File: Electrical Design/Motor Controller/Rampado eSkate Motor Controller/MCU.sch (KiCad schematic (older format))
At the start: 12 parts

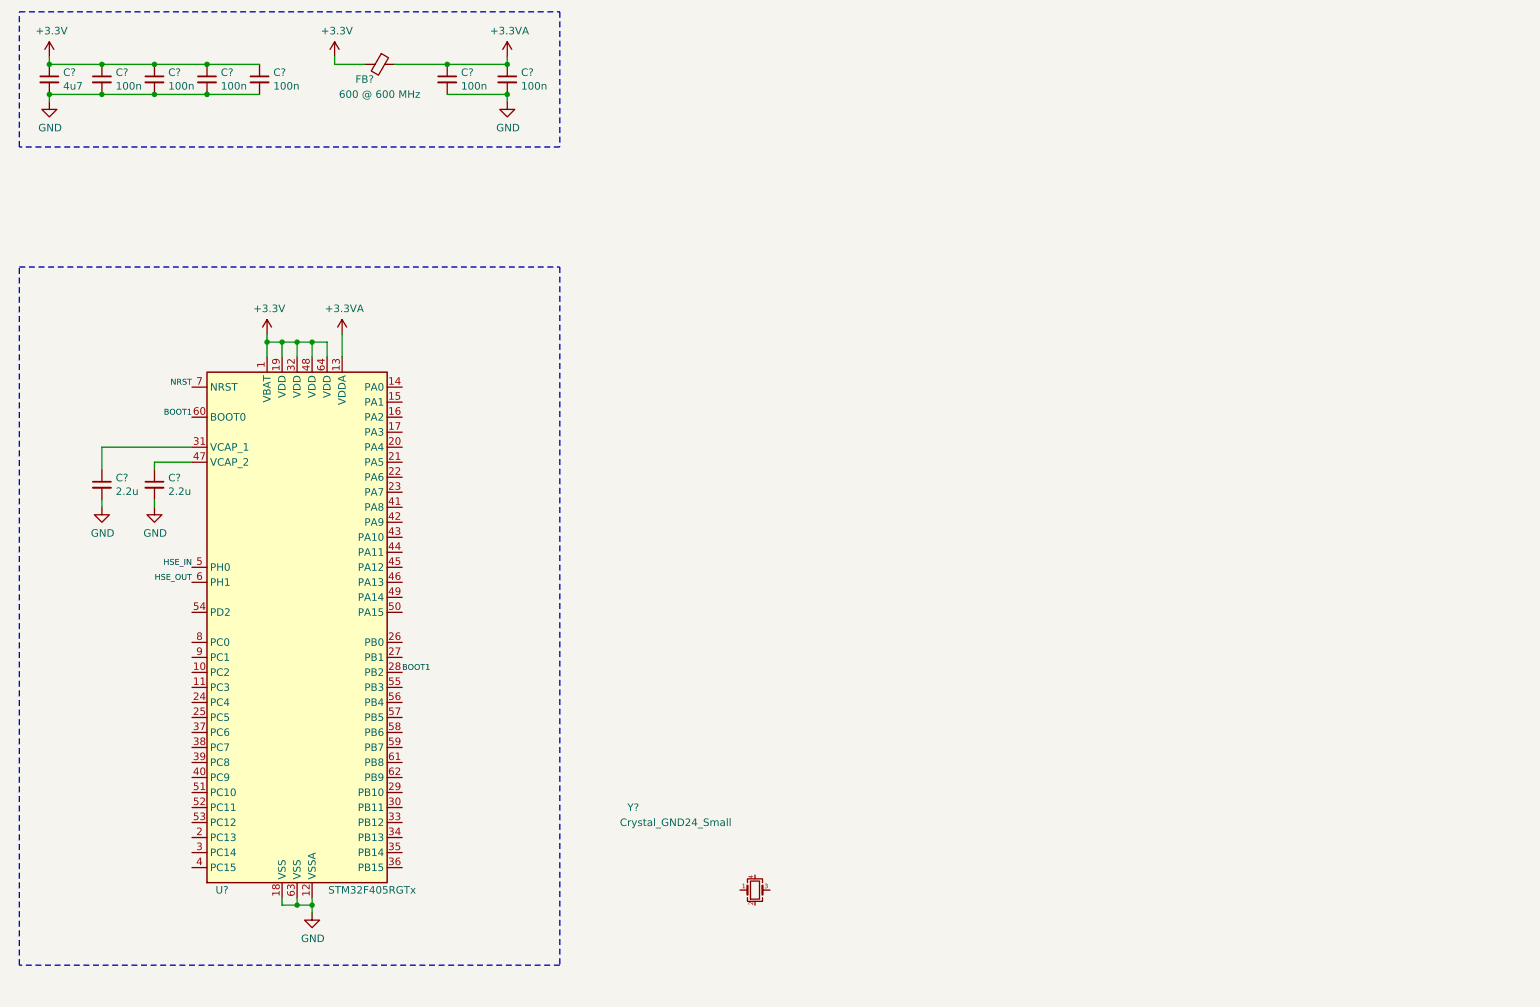
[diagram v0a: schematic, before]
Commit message: Finished USB and started peripherals for motor controller
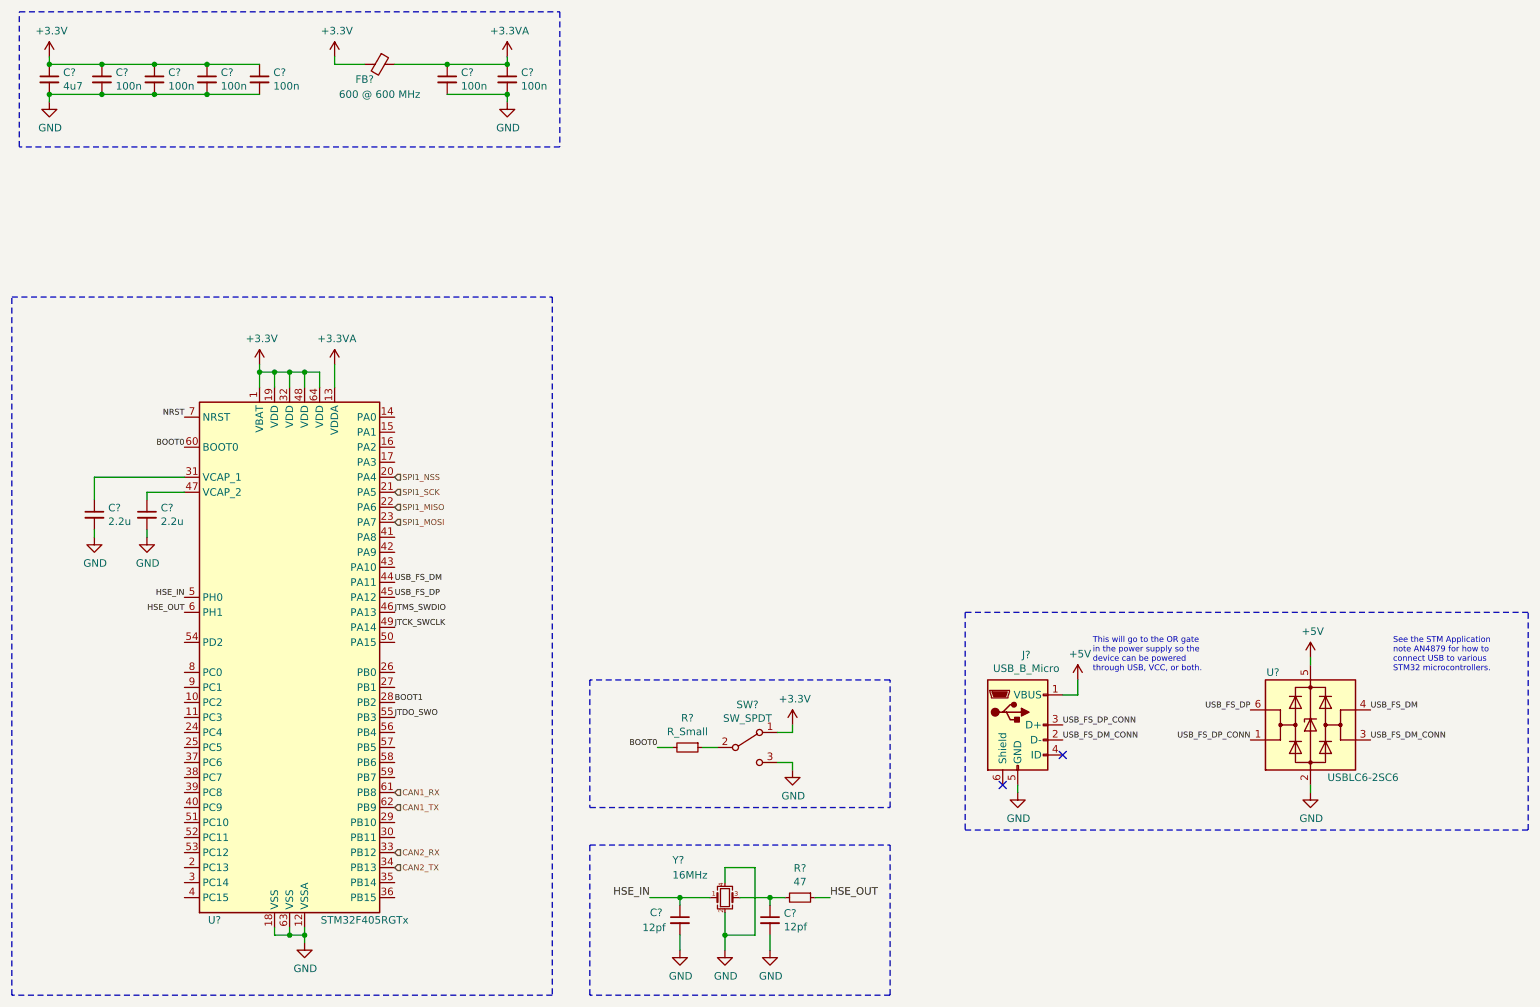
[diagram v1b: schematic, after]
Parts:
- added C? (x2): 12pf, symbol Device:C_Small
- added J?: USB_B_Micro, symbol Connector:USB_B_Micro
- added R?: 47, symbol Device:R_Small
- added R?: R_Small, symbol Device:R_Small
- added SW?: SW_SPDT, symbol Switch:SW_SPDT
- added U?: USBLC6-2SC6, Package_TO_SOT_SMD:SOT-23-6, symbol Power_Protection:USBLC6-2SC6
- Y?: value Crystal_GND24_Small -> 16MHz
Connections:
- net +3V3: now also SW?.1 (A)
- net BOOT1: no longer U?.60 (BOOT0)
- net GND: now also Y?.2, Y?.4, C?.2, C?.2, J?.5 (GND), SW?.3 (C), U?.2 (GND)
- net HSE_IN: now also Y?.1, C?.1
- net HSE_OUT: now also R?.1
- net SPI1_NSS: now reaches U?.20 (PA4)
- net SPI1_SCK: now reaches U?.21 (PA5)
- net SPI1_MISO: now reaches U?.22 (PA6)
- net SPI1_MOSI: now reaches U?.23 (PA7)
- net CAN2_RX: now reaches U?.33 (PB12)
- net CAN2_TX: now reaches U?.34 (PB13)
- net USB_FS_DM: now reaches U?.44 (PA11)
- net USB_FS_DM: now also U?.4 (I/O2)
- net USB_FS_DP: now reaches U?.45 (PA12)
- net USB_FS_DP: now also U?.6 (I/O1)
- net JTMS_SWDIO: now reaches U?.46 (PA13)
- net JTCK_SWCLK: now reaches U?.49 (PA14)
- net JTDO_SWO: now reaches U?.55 (PB3)
- net CAN1_RX: now reaches U?.61 (PB8)
- net CAN1_TX: now reaches U?.62 (PB9)
- net at Y?.3: now also C?.1, R?.2
- new net: R?.1, SW?.2 (B)
- new net +5V: J?.1 (VBUS), U?.5 (VBUS)
- new net BOOT0: R?.2, U?.60 (BOOT0)
- new net USB_FS_DM_CONN: J?.2 (D-), U?.3 (I/O2)
- new net USB_FS_DP_CONN: J?.3 (D+), U?.1 (I/O1)
- no-connect marks 0 -> 2
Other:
- note added: "See the STM Application \nnote AN4879 for how to \nconnect USB to various \nSTM32 microcontrollers."
- note added: "This will go to the OR gate \nin the power supply so the \ndevice can be powered \nthrough USB, VCC, or both."
- moved on the sheet: C?, U?, Y?
